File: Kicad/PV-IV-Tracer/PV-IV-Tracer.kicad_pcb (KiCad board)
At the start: 2 copper layers, 59 parts, among them J1 Conn_01x04_Male, J2 Conn_01x03_Male, J3 Conn_01x02_Male, Q1 Q_NMOS_GDS, Q2 BC817, Q3 BD139, U1 MCP4821, U2 Opamp_Dual, U3 ATmega8L-8P, U4 LM555xN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

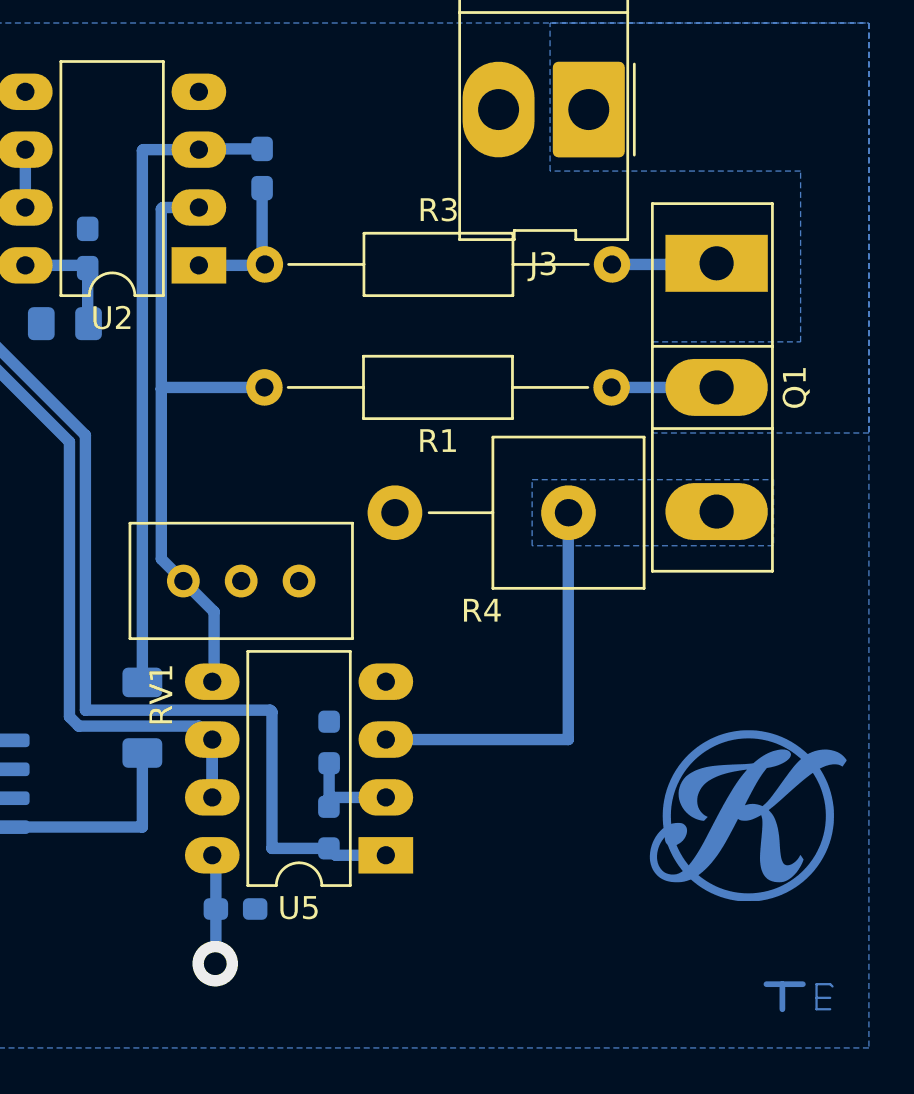
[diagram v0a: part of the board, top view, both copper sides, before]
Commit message: V2 PCB swaped the opamp so that the inverting input is coneected to the setpoint changed PCB layout.
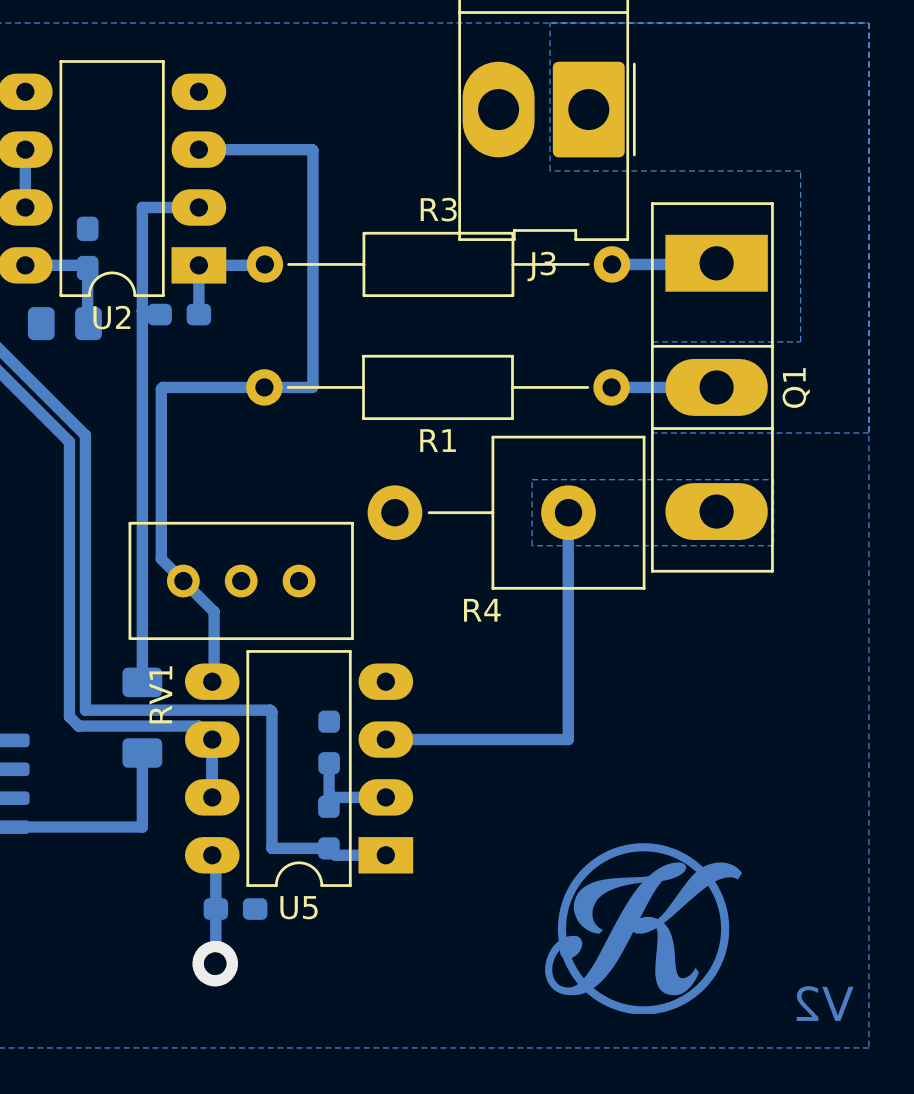
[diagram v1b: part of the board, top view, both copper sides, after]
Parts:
- moved C4 7.37 mm to (59.7, 97.8), turned to 0 degrees
- moved G*** 6.76 mm to (80.4, 126.0)
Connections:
- U2 pad 2: Net-(R1-Pad2) -> Net-(C4-Pad1)
- U2 pad 3: Net-(C4-Pad1) -> Net-(R1-Pad2)
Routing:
- net Net-(R1-Pad2): track 28.1 -> 36.0 mm
- net (no net): track 5.74 -> 0.00 mm
- net Net-(C4-Pad1): track 28.6 -> 24.3 mm
- net Net-(C4-Pad2): track 6.99 -> 5.86 mm
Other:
- board text added: "V2"
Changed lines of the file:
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@@
   (net 34 "Net-(U2-Pad6)")
   (net 35 "Net-(C25-Pad1)")
-  (net 36 "Net-(R9-Pad2)")
+  (net 36 "Net-(Q3-Pad3)")
   (net 37 "Net-(R12-Pad1)")
   (footprint "Package_DIP:DIP-8_W7.62mm_LongPads" (layer "F.Cu")
@@
       (net 5 "Net-(C4-Pad2)") (pintype "output"))
     (pad "2" thru_hole oval (at 0 2.54 180) (size 2.4 1.6) (drill 0.8) (layers *.Cu *.Mask)
-      (net 24 "Net-(R1-Pad2)") (pinfunction "-") (pintype "input"))
+      (net 4 "Net-(C4-Pad1)") (pinfunction "-") (pintype "input"))
     (pad "3" thru_hole oval (at 0 5.08 180) (size 2.4 1.6) (drill 0.8) (layers *.Cu *.Mask)
-      (net 4 "Net-(C4-Pad1)") (pinfunction "+") (pintype "input"))
+      (net 24 "Net-(R1-Pad2)") (pinfunction "+") (pintype "input"))
     (pad "4" thru_hole oval (at 0 7.62 180) (size 2.4 1.6) (drill 0.8) (layers *.Cu *.Mask)
       (net 2 "GND") (pinfunction "V-") (pintype "power_in"))
@@
   )
   (footprint "logo:logo" (layer "F.Cu")
-    (at 84.992977 120.99219)
+    (at 80.392977 125.95219)
     (attr smd board_only exclude_from_pos_files exclude_from_bom)
     (fp_text reference "G***" (at 0 0) (layer "F.SilkS") hide
@@
       (net 26 "Net-(D1-Pad2)") (pinfunction "C") (pintype "passive"))
     (pad "3" thru_hole oval (at 5.08 0 90) (size 1.8 1.8) (drill 1) (layers *.Cu *.Mask)
-      (net 36 "Net-(R9-Pad2)") (pinfunction "B") (pintype "input"))
+      (net 36 "Net-(Q3-Pad3)") (pinfunction "B") (pintype "input"))
     (model "${KICAD6_3DMODEL_DIR}/Package_TO_SOT_THT.3dshapes/TO-126-3_Vertical.wrl"
       (offset (xyz 0 0 0))
@@
   )
   (footprint "Capacitor_SMD:C_0603_1608Metric_Pad1.08x0.95mm_HandSolder" (layer "B.Cu")
-    (at 63.3575 91.39 -90)
+    (at 59.72 97.8)
     (descr "Capacitor SMD 0603 (1608 Metric), square (rectangular) end terminal, IPC_7351 nominal with elongated pad for handsoldering. (Body size source: IPC-SM-782 page 76, https://www.pcb-3d.com/wordpress/wp-content/uploads/ipc-sm-782a_amendment_1_and_2.pdf), generated with kicad-footprint-generator")
     (tags "capacitor handsolder")
@@
     (property "Sheetname" "")
     (attr smd)
-    (fp_text reference "C4" (at 0 1.43 90) (layer "B.SilkS")
+    (fp_text reference "C4" (at 0 1.43) (layer "B.SilkS")
       (effects (font (size 1 1) (thickness 0.15)) (justify mirror))
     )
-    (fp_text value "1n" (at 0 -1.43 90) (layer "B.Fab")
+    (fp_text value "1n" (at 0 -1.43) (layer "B.Fab")
       (effects (font (size 1 1) (thickness 0.15)) (justify mirror))
     )
-    (fp_text user "${REFERENCE}" (at 0 0 90) (layer "B.Fab")
+    (fp_text user "${REFERENCE}" (at 0 0) (layer "B.Fab")
       (effects (font (size 0.4 0.4) (thickness 0.06)) (justify mirror))
     )
@@
     (fp_line (start -0.8 -0.4) (end -0.8 0.4) (layer "B.Fab") (width 0.1))
     (fp_line (start 0.8 0.4) (end 0.8 -0.4) (layer "B.Fab") (width 0.1))
-    (pad "1" smd roundrect (at -0.8625 0 270) (size 1.075 0.95) (layers "B.Cu" "B.Paste" "B.Mask") (roundrect_rratio 0.25)
+    (pad "1" smd roundrect (at -0.8625 0) (size 1.075 0.95) (layers "B.Cu" "B.Paste" "B.Mask") (roundrect_rratio 0.25)
       (net 4 "Net-(C4-Pad1)") (pintype "passive"))
-    (pad "2" smd roundrect (at 0.8625 0 270) (size 1.075 0.95) (layers "B.Cu" "B.Paste" "B.Mask") (roundrect_rratio 0.25)
+    (pad "2" smd roundrect (at 0.8625 0) (size 1.075 0.95) (layers "B.Cu" "B.Paste" "B.Mask") (roundrect_rratio 0.25)
       (net 5 "Net-(C4-Pad2)") (pintype "passive"))
     (model "${KICAD6_3DMODEL_DIR}/Capacitor_SMD.3dshapes/C_0603_1608Metric.wrl"
@@
       (net 29 "Net-(R9-Pad1)") (pintype "passive"))
     (pad "2" smd roundrect (at 1.55 0 270) (size 1.3 1.75) (layers "B.Cu" "B.Paste" "B.Mask") (roundrect_rratio 0.1923076923)
-      (net 36 "Net-(R9-Pad2)") (pintype "passive"))
+      (net 36 "Net-(Q3-Pad3)") (pintype "passive"))
     (model "${KICAD6_3DMODEL_DIR}/Resistor_SMD.3dshapes/R_1206_3216Metric.wrl"
       (offset (xyz 0 0 0))
@@
     )
   )
+  (gr_text "V2" (at 87.98 128.12) (layer "B.Cu")
+    (effects (font (size 1.5 1.5) (thickness 0.3)) (justify mirror))
+  )
   (dimension (type aligned) (layer "Dwgs.User")
     (pts (xy 36.8 52.2) (xy 71.8 52.2))
@@
     (style (thickness 0.15) (arrow_length 1.27) (text_position_mode 0) (extension_height 0.58642) (extension_offset 0.5) keep_text_aligned)
   )
-  (segment (start 86.2 127.2) (end 86.2 128.3) (width 0.25) (layer "B.Cu") (net 0))
-  (segment (start 87.7 127.8) (end 87.7 127.2) (width 0.1) (layer "B.Cu") (net 0))
-  (segment (start 87.7 128.3) (end 88.3 128.3) (width 0.1) (layer "B.Cu") (net 0))
-  (segment (start 88.3 127.2) (end 88.4 127.3) (width 0.1) (layer "B.Cu") (net 0))
-  (segment (start 87.1 127.2) (end 86.2 127.2) (width 0.25) (layer "B.Cu") (net 0))
-  (segment (start 87.7 127.8) (end 88.3 127.8) (width 0.1) (layer "B.Cu") (net 0))
-  (segment (start 87.7 128.3) (end 87.7 127.8) (width 0.1) (layer "B.Cu") (net 0))
-  (segment (start 86.2 127.2) (end 85.5 127.2) (width 0.25) (layer "B.Cu") (net 0))
-  (segment (start 87.7 127.2) (end 88.3 127.2) (width 0.1) (layer "B.Cu") (net 0))
   (via (at 56.6 72.3) (size 2.5) (drill 1) (layers "F.Cu" "B.Cu") (free) (net 1))
   (via (at 68.5 72.2) (size 2.5) (drill 1) (layers "F.Cu" "B.Cu") (free) (net 1))
@@
   (segment (start 47.2375 123.675) (end 47.3625 123.8) (width 0.5) (layer "B.Cu") (net 3))
   (segment (start 51.035 117.765) (end 52.175 117.765) (width 0.5) (layer "B.Cu") (net 3))
-  (segment (start 58.1 90.6) (end 58.1 113.95) (width 0.5) (layer "B.Cu") (net 4))
-  (segment (start 60.615 90.5275) (end 60.5825 90.56) (width 0.5) (layer "B.Cu") (net 4))
-  (segment (start 60.5825 90.56) (end 58.14 90.56) (width 0.5) (layer "B.Cu") (net 4))
-  (segment (start 58.14 90.56) (end 58.1 90.6) (width 0.5) (layer "B.Cu") (net 4))
-  (segment (start 63.3575 90.5275) (end 60.615 90.5275) (width 0.5) (layer "B.Cu") (net 4))
+  (segment (start 58.24 97.8) (end 58.1 97.66) (width 0.5) (layer "B.Cu") (net 4))
+  (segment (start 58.1 97.66) (end 58.1 113.95) (width 0.5) (layer "B.Cu") (net 4))
+  (segment (start 58.1 93.1) (end 58.1 97.66) (width 0.5) (layer "B.Cu") (net 4))
+  (segment (start 58.8575 97.8) (end 58.24 97.8) (width 0.5) (layer "B.Cu") (net 4))
+  (segment (start 58.1 93.1) (end 60.5825 93.1) (width 0.5) (layer "B.Cu") (net 4))
+  (segment (start 60.6825 93.1) (end 60.5825 93) (width 0.5) (layer "B.Cu") (net 4))
+  (segment (start 60.5825 95.64) (end 60.5825 97.8) (width 0.5) (layer "B.Cu") (net 5))
   (segment (start 60.5825 95.64) (end 59.795 95.64) (width 0.5) (layer "B.Cu") (net 5))
-  (segment (start 63.3575 92.2525) (end 63.3575 95.54) (width 0.5) (layer "B.Cu") (net 5))
   (segment (start 63.44 95.64) (end 63.48 95.6) (width 0.5) (layer "B.Cu") (net 5))
   (segment (start 60.5825 95.64) (end 63.44 95.64) (width 0.5) (layer "B.Cu") (net 5))
@@
   (segment (start 58.9325 101.0675) (end 58.9325 108.5325) (width 0.5) (layer "B.Cu") (net 24))
   (segment (start 63.46 101) (end 59 101) (width 0.5) (layer "B.Cu") (net 24))
-  (segment (start 59 93.1) (end 58.9325 93.1675) (width 0.5) (layer "B.Cu") (net 24))
-  (segment (start 58.9325 93.1675) (end 58.9325 101.0675) (width 0.5) (layer "B.Cu") (net 24))
+  (segment (start 65.55 90.56) (end 65.59 90.6) (width 0.5) (layer "B.Cu") (net 24))
+  (segment (start 60.615 90.5275) (end 60.5825 90.56) (width 0.5) (layer "B.Cu") (net 24))
+  (segment (start 65.58 101) (end 63.46 101) (width 0.5) (layer "B.Cu") (net 24))
   (segment (start 61.25 110.85) (end 61.25 113.84) (width 0.5) (layer "B.Cu") (net 24))
   (segment (start 59 101) (end 58.9325 101.0675) (width 0.5) (layer "B.Cu") (net 24))
-  (segment (start 60.5825 93.1) (end 59 93.1) (width 0.5) (layer "B.Cu") (net 24))
+  (segment (start 65.59 90.6) (end 65.59 100.92) (width 0.5) (layer "B.Cu") (net 24))
+  (segment (start 65.59 100.92) (end 65.53 100.98) (width 0.5) (layer "B.Cu") (net 24))
+  (segment (start 60.5825 90.56) (end 65.55 90.56) (width 0.5) (layer "B.Cu") (net 24))
   (segment (start 58.9325 108.5325) (end 61.25 110.85) (width 0.5) (layer "B.Cu") (net 24))
-  (segment (start 60.6825 93.1) (end 60.5825 93) (width 0.5) (layer "B.Cu") (net 24))
   (segment (start 58.57 58.1625) (end 58.58 58.1725) (width 0.5) (layer "B.Cu") (net 25))
   (segment (start 56.1625 58.2) (end 58.5525 58.2) (width 0.5) (layer "B.Cu") (net 25))
